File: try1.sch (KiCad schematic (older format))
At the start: 21 parts, among them J10 Archon-connector-modules-Driv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, J11 Archon-connector-modules-Driv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, J2 Archon-connector-modules-Heat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, J21 DB37, J22 DB37, J3 Archon-connector-modules-Driv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, J31 DB9, J4 Archon-connector-modules-LVBi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, J41 CONN_DVI, J5 Archon-connector-modules-ADC, J6 Archon-connector-modules-ADC, J7 Archon-connector-modules-ADC, J8 Archon-connector-modules-ADC, J9 Archon-connector-modules-HVBi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

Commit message: Label extra ADC MOD6 card for furture use.
I intend to pull these out to spare pads.
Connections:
- net labels added: ADC5_GND1, ADC5_GND2, ADC6_CH1_N, ADC6_CH1_P, ADC6_CH2_N, ADC6_CH2_P, ADC6_CH3_N, ADC6_CH3_P, ADC6_CH4_N, ADC6_CH4_P, ADC6_GND1, ADC6_GND2, DRV10_GND1, DRV10_GND2, DRV11_GND1, DRV11_GND2
- no-connect marks 310 -> 314
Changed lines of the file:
@@
 NoConn ~ 25900 13350
 NoConn ~ 26800 13350
+Text GLabel 11550 13450 0    60   Input ~ 0
+ADC5_GND1
+Text GLabel 12600 13450 2    60   Input ~ 0
+ADC5_GND2
+Text GLabel 25900 13350 0    60   Input ~ 0
+DRV10_GND1
+Text GLabel 26800 13350 2    60   Input ~ 0
+DRV10_GND2
+Text GLabel 28700 13350 0    60   Input ~ 0
+DRV11_GND1
+Text GLabel 29600 13350 2    60   Input ~ 0
+DRV11_GND2
+Text GLabel 16200 12350 2    60   Input ~ 0
+ADC6_CH1_N
+Text GLabel 16200 12450 2    60   Input ~ 0
+ADC6_CH1_P
+Text GLabel 16200 12650 2    60   Input ~ 0
+ADC6_CH2_N
+Text GLabel 16200 12750 2    60   Input ~ 0
+ADC6_CH2_P
+Text GLabel 16200 12950 2    60   Input ~ 0
+ADC6_CH3_N
+Text GLabel 16200 13050 2    60   Input ~ 0
+ADC6_CH3_P
+Text GLabel 16200 13250 2    60   Input ~ 0
+ADC6_CH4_N
+Text GLabel 16200 13350 2    60   Input ~ 0
+ADC6_CH4_P
+Text GLabel 16200 13450 2    60   Input ~ 0
+ADC6_GND2
+NoConn ~ 16200 12250
+NoConn ~ 16200 12550
+NoConn ~ 16200 12850
+NoConn ~ 16200 13150
+Text GLabel 15150 13450 0    60   Input ~ 0
+ADC6_GND1
 $EndSCHEMATC

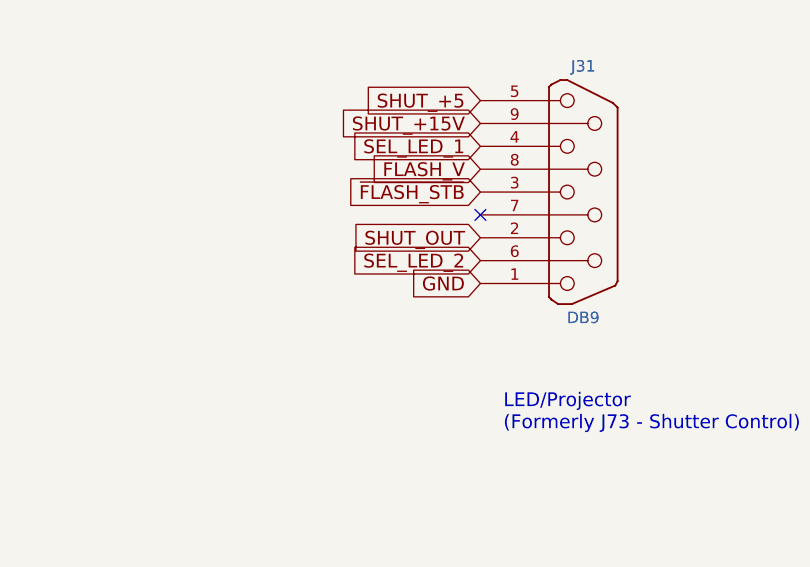
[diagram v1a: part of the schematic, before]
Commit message: Rename GND pin on Shutter Connector
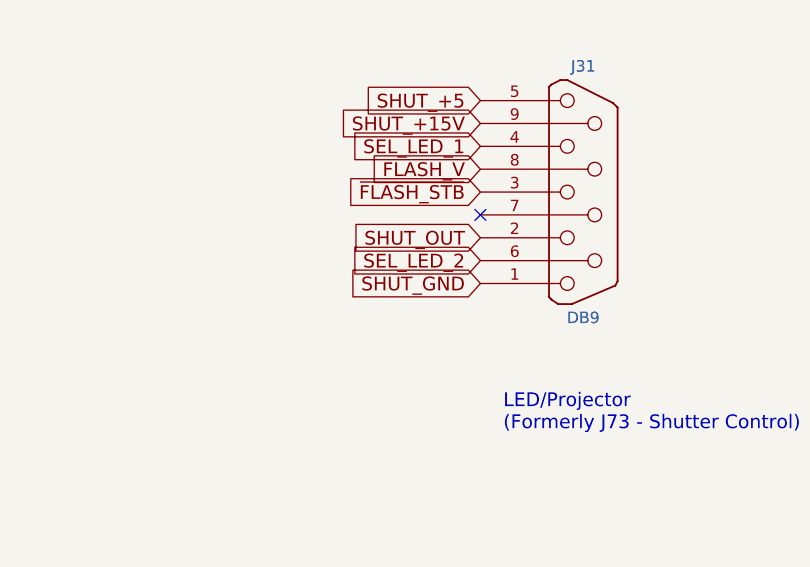
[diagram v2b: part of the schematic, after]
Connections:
- net labels added: SHUT_GND
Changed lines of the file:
@@
 NoConn ~ 24250 5550
 Text GLabel 4000 4600 0    60   Input ~ 0
-GND
+SHUT_GND
 Text GLabel 4000 4400 0    60   Input ~ 0
 SHUT_OUT

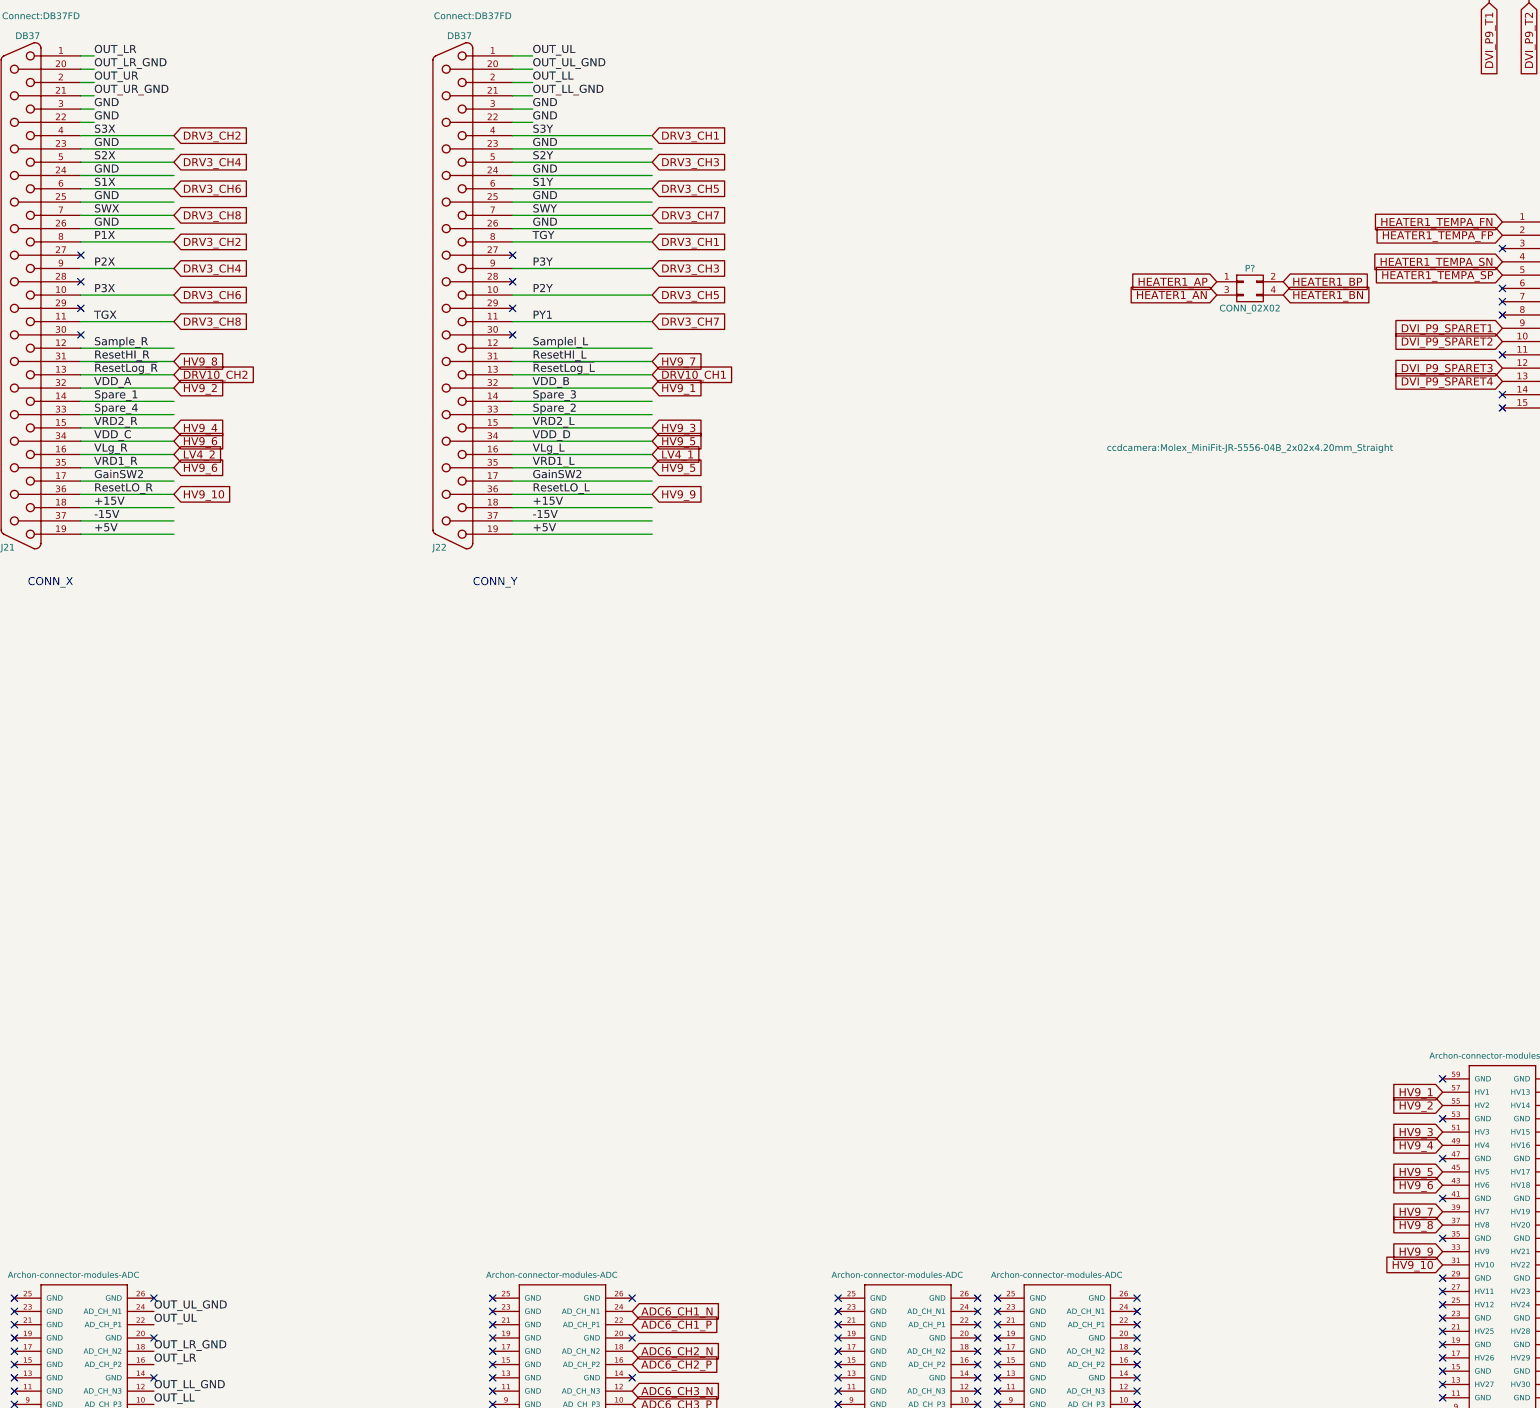
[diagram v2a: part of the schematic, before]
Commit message: Update Dewar PINs
Changed GND to connector-specific names.
Connect 5V,15V,&-15V to bias modules.
Change GainSW2 name to connector-specific names.
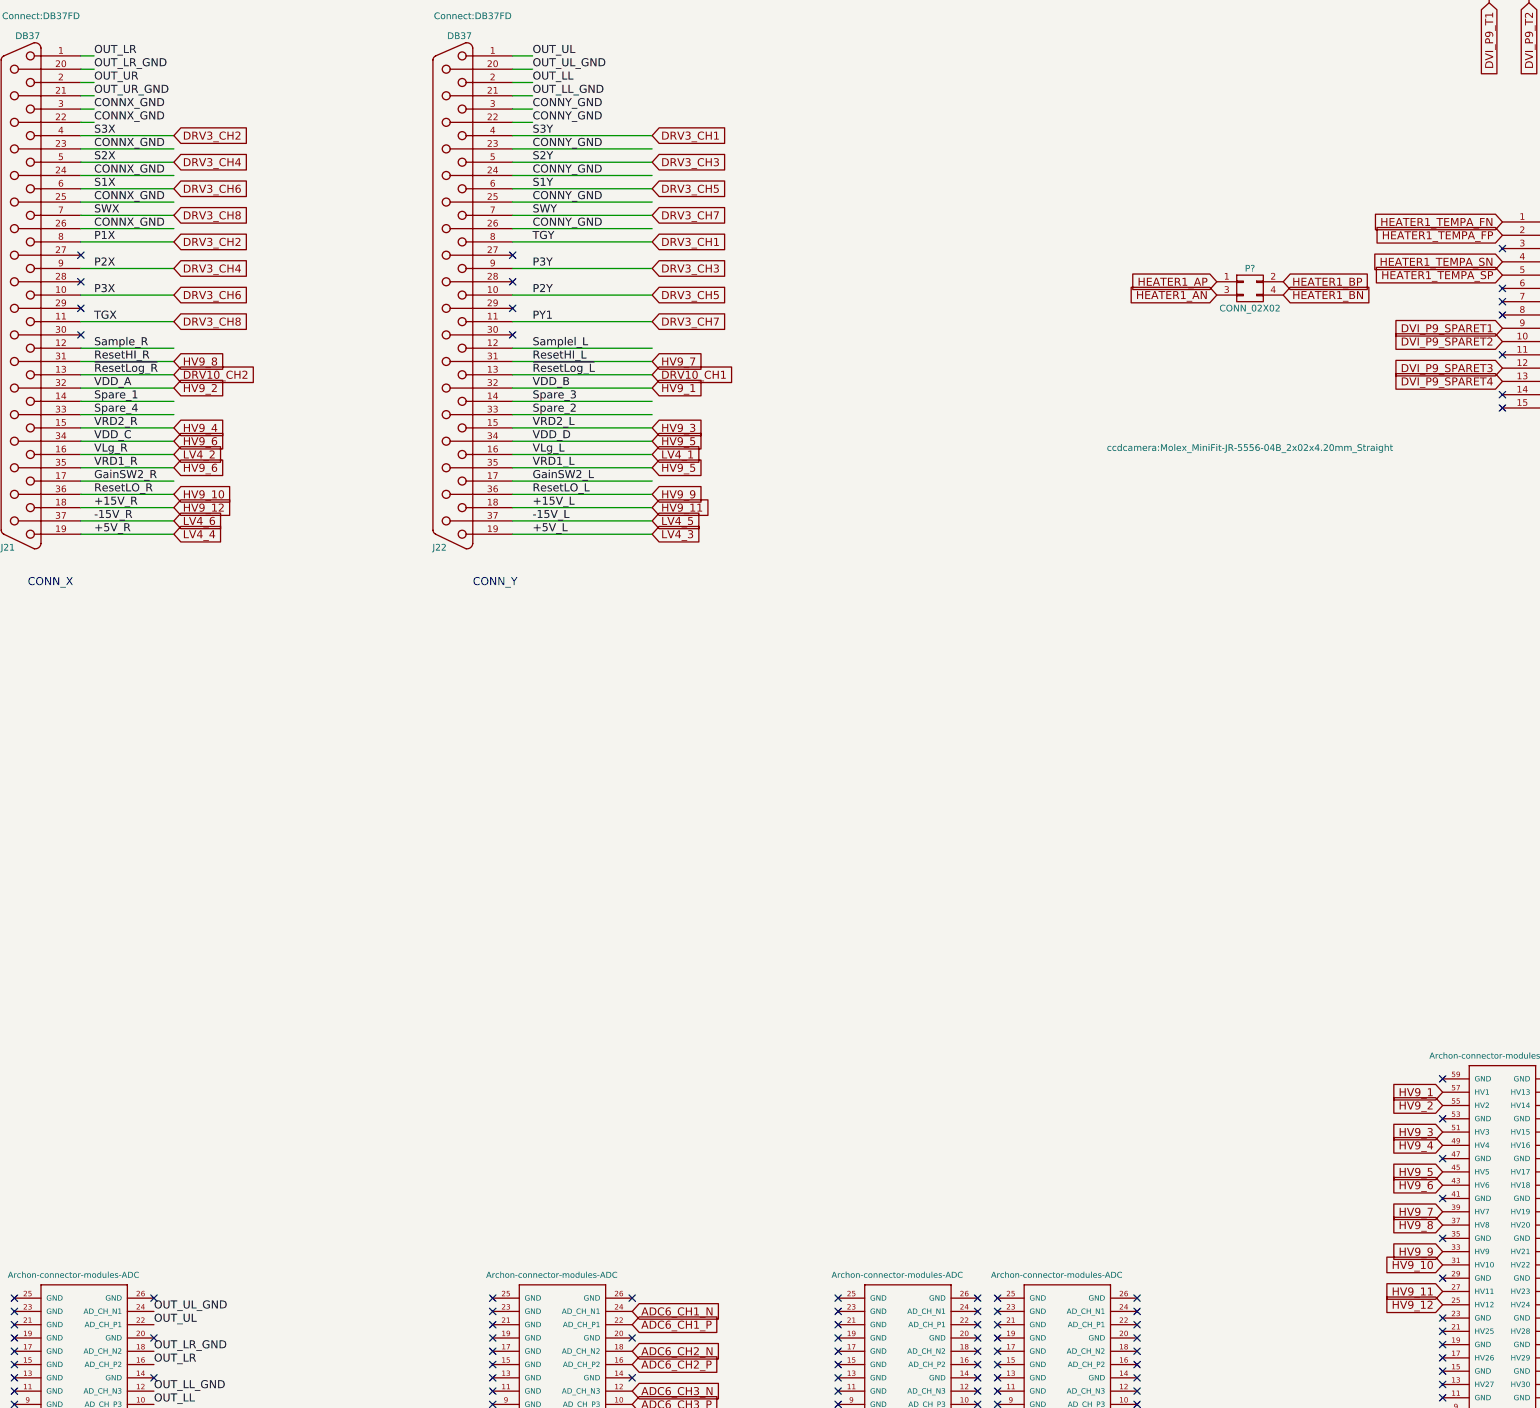
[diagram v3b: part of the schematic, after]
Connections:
- net labels added: +15V_L, +15V_R, +5V_L, +5V_R, -15V_L, -15V_R, CONNX_GND, CONNY_GND, GainSW2_L, GainSW2_R, HV9_11, HV9_12
- net labels removed: +15V, +5V, -15V, GND, GainSW2
- no-connect marks 314 -> 312
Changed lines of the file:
@@
 OUT_LL_GND
 Text Label 15450 3300 0    60   ~ 0
-GND
+CONNY_GND
 Text Label 15450 3400 0    60   ~ 0
-GND
+CONNY_GND
 Text Label 15450 3500 0    60   ~ 0
 S3Y
 Text Label 15450 3600 0    60   ~ 0
-GND
+CONNY_GND
 Text Label 15450 3700 0    60   ~ 0
 S2Y
 Text Label 15450 3800 0    60   ~ 0
-GND
+CONNY_GND
 Text Label 15450 3900 0    60   ~ 0
 S1Y
 Text Label 15450 4000 0    60   ~ 0
-GND
+CONNY_GND
 Text Label 15450 4100 0    60   ~ 0
 SWY
 Text Label 15450 4200 0    60   ~ 0
-GND
+CONNY_GND
 Text Label 15450 4300 0    60   ~ 0
 TGY
@@
 VRD1_L
 Text Label 15450 6100 0    60   ~ 0
-GainSW2
+GainSW2_L
 Text Label 15450 6200 0    60   ~ 0
 ResetLO_L
 Text Label 15450 6300 0    60   ~ 0
-+15V
++15V_L
 Text Label 15450 6400 0    60   ~ 0
--15V
+-15V_L
 Text Label 15450 6500 0    60   ~ 0
-+5V
++5V_L
 NoConn ~ 12050 4600
 NoConn ~ 12050 5000
@@
 OUT_UR_GND
 Text Label 12150 3300 0    60   ~ 0
-GND
+CONNX_GND
 Text Label 12150 3400 0    60   ~ 0
-GND
+CONNX_GND
 Text Label 12150 3500 0    60   ~ 0
 S3X
 Text Label 12150 3600 0    60   ~ 0
-GND
+CONNX_GND
 Text Label 12150 3700 0    60   ~ 0
 S2X
 Text Label 12150 3800 0    60   ~ 0
-GND
+CONNX_GND
 Text Label 12150 3900 0    60   ~ 0
 S1X
 Text Label 12150 4000 0    60   ~ 0
-GND
+CONNX_GND
 Text Label 12150 4100 0    60   ~ 0
 SWX
 Text Label 12150 4200 0    60   ~ 0
-GND
+CONNX_GND
 Text Label 12150 4300 0    60   ~ 0
 P1X
@@
 VRD1_R
 Text Label 12150 6100 0    60   ~ 0
-GainSW2
+GainSW2_R
 Text Label 12150 6200 0    60   ~ 0
 ResetLO_R
 Text Label 12150 6300 0    60   ~ 0
-+15V
++15V_R
 Text Label 12150 6400 0    60   ~ 0
--15V
+-15V_R
 Text Label 12150 6500 0    60   ~ 0
-+5V
++5V_R
 NoConn ~ 23200 13200
 NoConn ~ 23200 13300
@@
 NoConn ~ 22300 11800
 NoConn ~ 22300 12100
-NoConn ~ 22300 12200
-NoConn ~ 22300 12300
 NoConn ~ 22300 12400
 NoConn ~ 22300 12500
@@
 Text GLabel 15150 13450 0    60   Input ~ 0
 ADC6_GND1
+Text GLabel 12750 6500 2    60   Input ~ 0
+LV4_4
+Text GLabel 16350 6500 2    60   Input ~ 0
+LV4_3
+Text GLabel 22300 12200 0    60   Input ~ 0
+HV9_11
+Text GLabel 22300 12300 0    60   Input ~ 0
+HV9_12
+Text GLabel 16350 6300 2    60   Input ~ 0
+HV9_11
+Text GLabel 12750 6300 2    60   Input ~ 0
+HV9_12
+Text GLabel 12750 6400 2    60   Input ~ 0
+LV4_6
+Text GLabel 16350 6400 2    60   Input ~ 0
+LV4_5
 $EndSCHEMATC

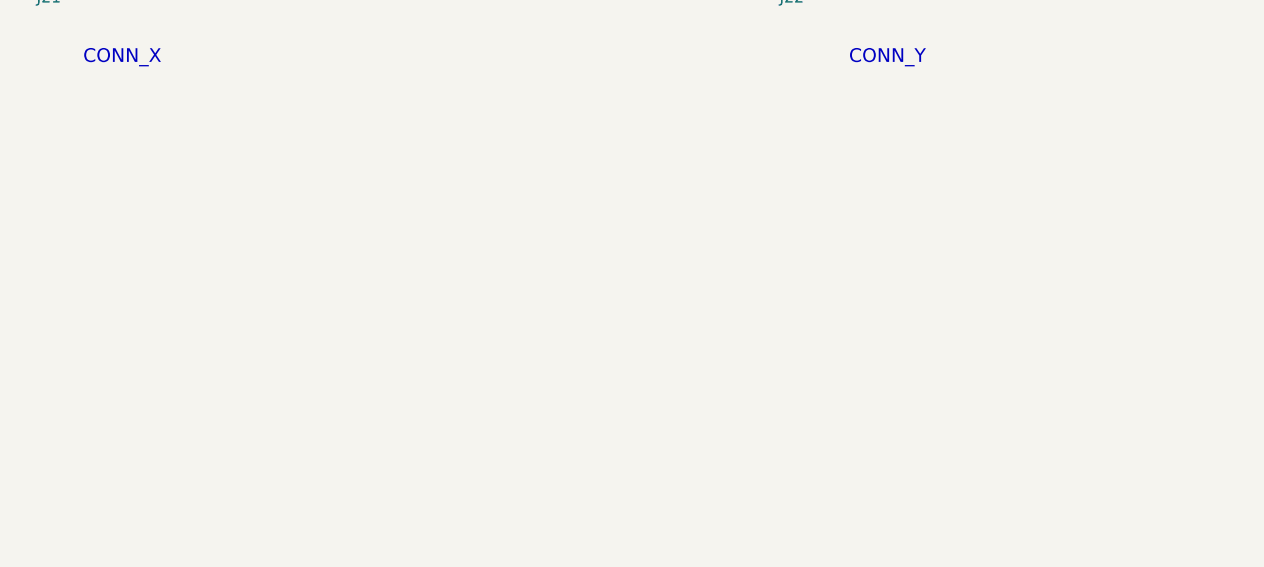
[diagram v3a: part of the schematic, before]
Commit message: Connect spare pins on dewar to pads
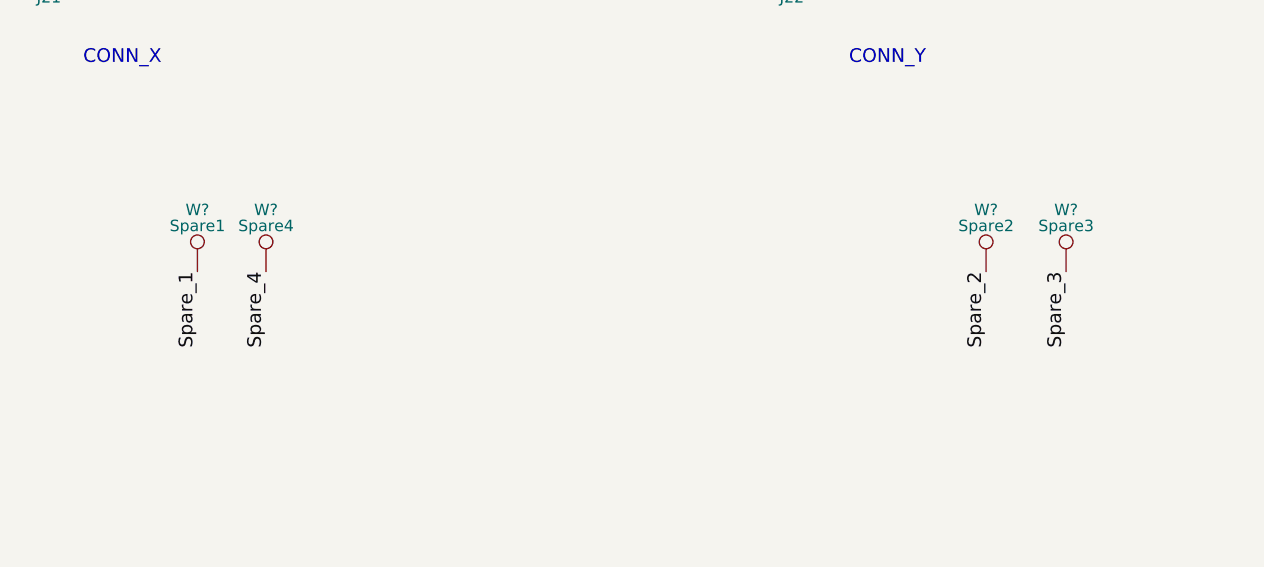
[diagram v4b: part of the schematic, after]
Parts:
- added W?: Spare1, symbol TEST_1P
- added W?: Spare4, symbol TEST_1P
- added W?: Spare3, symbol TEST_1P
- added W?: Spare2, symbol TEST_1P
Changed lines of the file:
@@
 Text GLabel 16350 6400 2    60   Input ~ 0
 LV4_5
+$Comp
+L TEST_1P W?
+U 1 1 57BED8F1
+P 12150 7800
+F 0 "W?" H 12150 8070 50  0000 C CNN
+F 1 "Spare1" H 12150 8000 50  0000 C CNN
+F 2 "" H 12350 7800 50  0000 C CNN
+F 3 "" H 12350 7800 50  0000 C CNN
+	1    12150 7800
+	1    0    0    -1
+$EndComp
+$Comp
+L TEST_1P W?
+U 1 1 57BEF217
+P 12450 7800
+F 0 "W?" H 12450 8070 50  0000 C CNN
+F 1 "Spare4" H 12450 8000 50  0000 C CNN
+F 2 "" H 12650 7800 50  0000 C CNN
+F 3 "" H 12650 7800 50  0000 C CNN
+	1    12450 7800
+	1    0    0    -1
+$EndComp
+$Comp
+L TEST_1P W?
+U 1 1 57BEF28B
+P 15950 7800
+F 0 "W?" H 15950 8070 50  0000 C CNN
+F 1 "Spare3" H 15950 8000 50  0000 C CNN
+F 2 "" H 16150 7800 50  0000 C CNN
+F 3 "" H 16150 7800 50  0000 C CNN
+	1    15950 7800
+	1    0    0    -1
+$EndComp
+$Comp
+L TEST_1P W?
+U 1 1 57BEF46D
+P 15600 7800
+F 0 "W?" H 15600 8070 50  0000 C CNN
+F 1 "Spare2" H 15600 8000 50  0000 C CNN
+F 2 "" H 15800 7800 50  0000 C CNN
+F 3 "" H 15800 7800 50  0000 C CNN
+	1    15600 7800
+	1    0    0    -1
+$EndComp
+Text Label 12150 7800 3    60   ~ 0
+Spare_1
+Text Label 12450 7800 3    60   ~ 0
+Spare_4
+Text Label 15600 7800 3    60   ~ 0
+Spare_2
+Text Label 15950 7800 3    60   ~ 0
+Spare_3
 $EndSCHEMATC

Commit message: Connect signal ground, add LED select jumper
Add hack to connect CCD signal ground to Driver module

Add jumper component for selection of LED in dewar, no yet connected

Added some text comments

Reposition Heater module
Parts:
- added JP? (x2): JUMPER, symbol JUMPER
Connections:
- net labels added: DRV3_GND, GND
- wire segments 66 -> 69
- no-connect marks 312 -> 314
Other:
- note added: "1: Blue/Red\n2: IR/Green"
- note added: "DVI Spare Pinouts"
- note added: "Signal Ground Connections for CCD"
- moved on the sheet: J2, J3
